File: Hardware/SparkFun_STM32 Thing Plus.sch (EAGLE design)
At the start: 67 parts, among them J3 QWIIC_RA, J6 CORTEX_DEBUG, J7 MICRO-SD, U1 MCP73831, U2 3.3V, U3 W25QXX128MBIT-6X5, U4 STM32F405RGT6, Y1 32.768kHz, Y2 12MHz

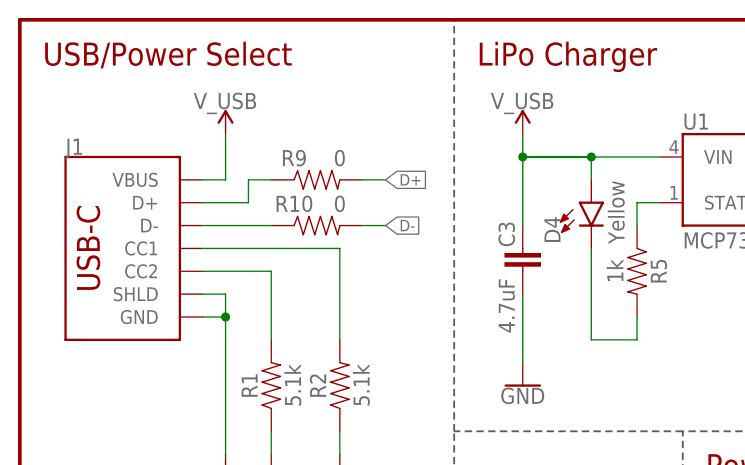
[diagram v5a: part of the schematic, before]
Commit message: Updated USB Load Resistors
Switch 0 ohm resistors back to 22 ohm
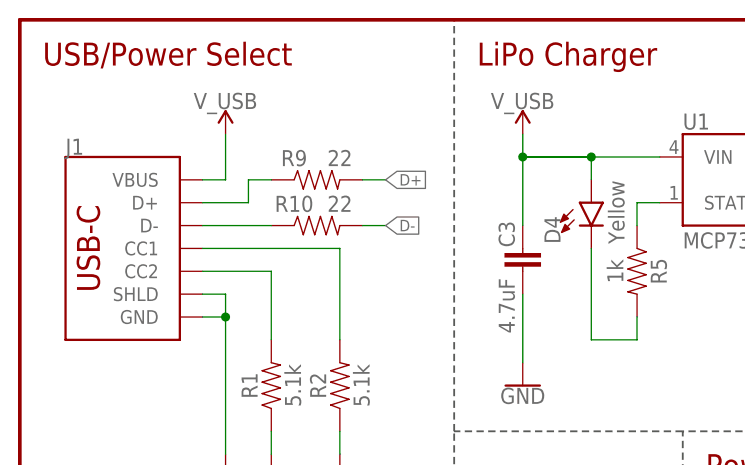
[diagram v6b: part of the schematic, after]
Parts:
- R10, R9: value 0 -> 22; device SparkFun-Resistors:0OHM-0603-1/10W -> SparkFun-Resistors:22OHM-0603-1/10W-1%
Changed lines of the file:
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@@
 <?xml version="1.0" encoding="utf-8"?>
 <!DOCTYPE eagle SYSTEM "eagle.dtd">
-<eagle version="9.5.2">
+<eagle version="9.6.2">
 <drawing>
 <settings>
@@
 <part name="GND28" library="SparkFun-PowerSymbols" deviceset="GND" device=""/>
 <part name="SUPPLY6" library="SparkFun-PowerSymbols" deviceset="V_USB" device=""/>
-<part name="R9" library="SparkFun-Resistors" deviceset="0OHM" device="-0603-1/10W" value="0"/>
-<part name="R10" library="SparkFun-Resistors" deviceset="0OHM" device="-0603-1/10W" value="0"/>
+<part name="R9" library="SparkFun-Resistors" deviceset="22OHM" device="-0603-1/10W-1%" value="22"/>
+<part name="R10" library="SparkFun-Resistors" deviceset="22OHM" device="-0603-1/10W-1%" value="22"/>
 <part name="GND36" library="SparkFun-PowerSymbols" deviceset="GND" device=""/>
 <part name="C20" library="SparkFun-Capacitors" deviceset="0.1UF" device="-0402T-10V-10%-X7R" value="0.1uF"/>
